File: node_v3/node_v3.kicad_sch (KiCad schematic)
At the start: 33 parts, among them J1 Conn_Coaxial, J10 Conn_01x02_Pin, J11 Conn_01x02_Pin, J2 Micro_SD_Card, J3 Conn_01x02_Pin, J4 Conn_01x02_Pin, J5 Conn_01x04_Pin, J6 Conn_01x02_Pin, J7 Conn_01x06_Pin, J8 Conn_01x04_Pin, J9 Conn_01x03_Pin, Q1 2N3904, U1 RFM69HCW, U2 Pico, U3 MCP73831-2-OT, U4 ADP2108AUJ-3.3, U5 CAT3200-5

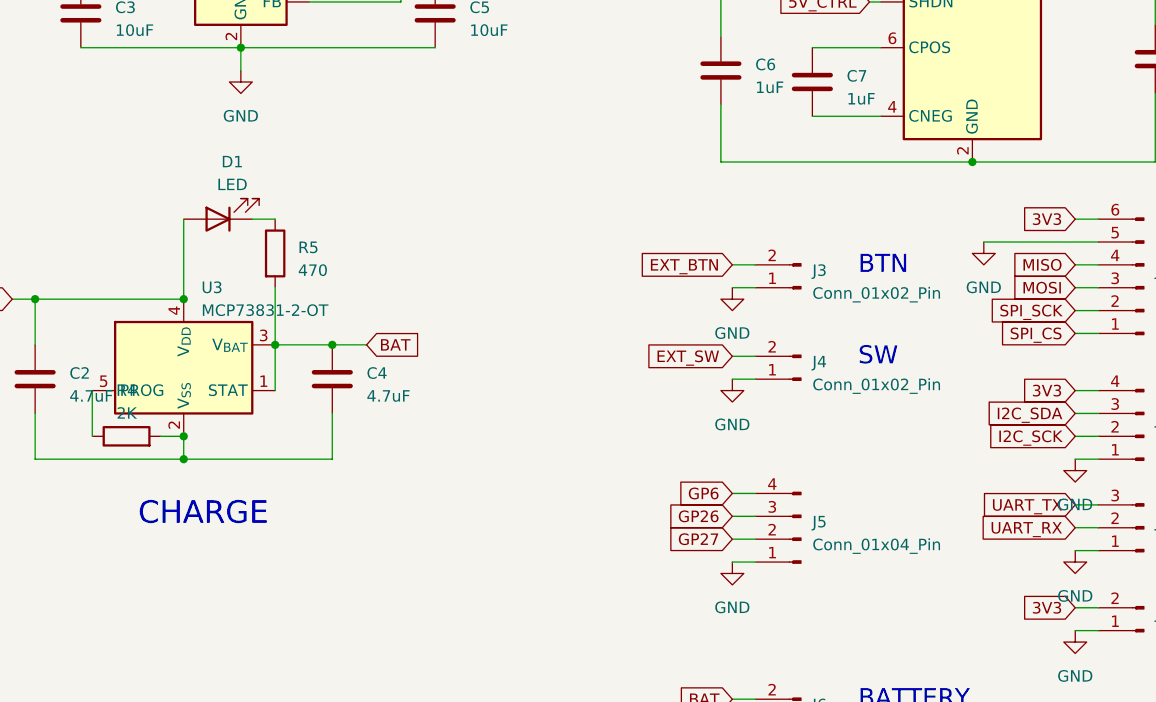
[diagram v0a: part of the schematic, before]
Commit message: added missing grounds
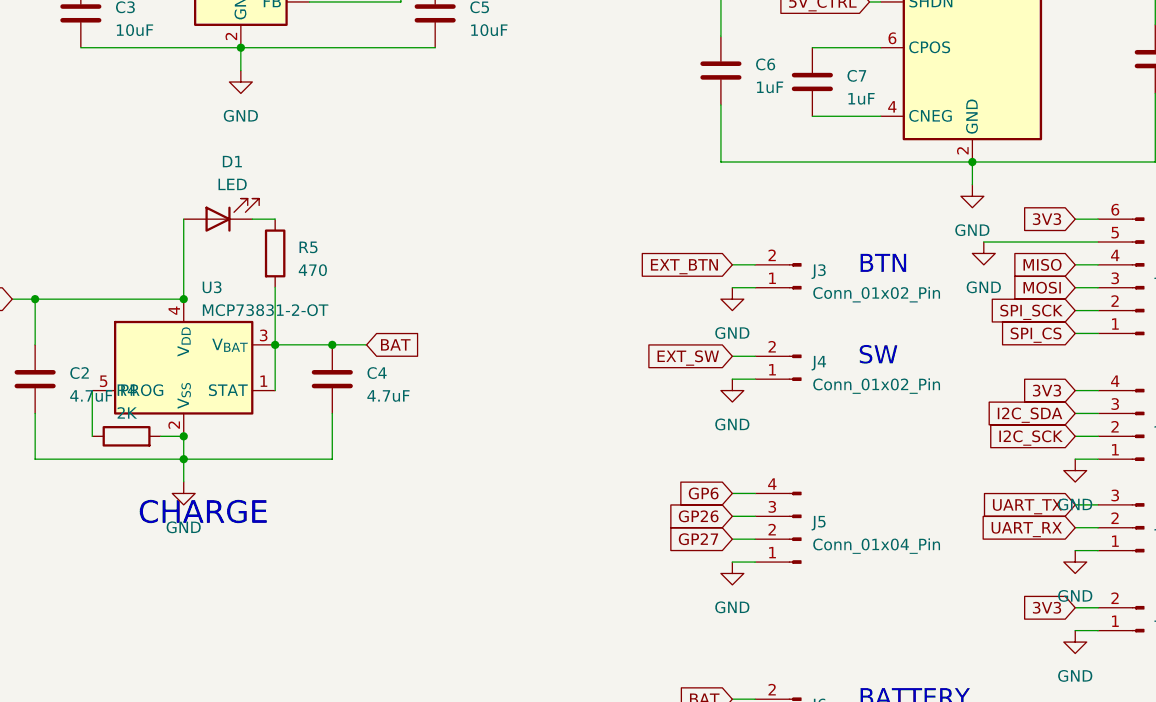
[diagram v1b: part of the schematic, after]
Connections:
- net GND: now also C2.2, C4.2, C6.2, C8.2, R4.2, U3.2 (V_{SS}), U5.2 (GND)
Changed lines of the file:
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@@
+    (stroke (width 0) (type default))
+  )
+  (wire (pts (xy 146.05 97.79) (xy 146.05 100.33))
     (stroke (width 0) (type default))
   )
@@
   )
   (wire (pts (xy 100.33 135.89) (xy 100.33 138.43))
+    (stroke (width 0) (type default))
+  )
+  (wire (pts (xy 233.68 64.77) (xy 233.68 67.31))
     (stroke (width 0) (type default))
   )
@@
         )
       )
+    )
+  )
+  (symbol (lib_id "power:GND") (at 233.68 67.31 0) (unit 1)
+    (in_bom yes) (on_board yes) (dnp no) (fields_autoplaced)
+    (property "Reference" "#PWR019" (at 233.68 73.66 0)
+      (effects (font (size 1.27 1.27)) hide)
+    )
+    (property "Value" "GND" (at 233.68 72.39 0)
+      (effects (font (size 1.27 1.27)))
+    )
+    (property "Footprint" "" (at 233.68 67.31 0)
+      (effects (font (size 1.27 1.27)) hide)
+    )
+    (property "Datasheet" "" (at 233.68 67.31 0)
+      (effects (font (size 1.27 1.27)) hide)
+    )
+    (pin "1")
+    (instances
+      (project "node_v3"
+        (path "/02682326-2508-4e7d-ab0e-a18e4bd4a5b6"
+          (reference "#PWR019") (unit 1)
+        )
+      )
+    )
+  )
+  (symbol (lib_id "power:GND") (at 146.05 100.33 0) (unit 1)
+    (in_bom yes) (on_board yes) (dnp no) (fields_autoplaced)
+    (property "Reference" "#PWR018" (at 146.05 106.68 0)
+      (effects (font (size 1.27 1.27)) hide)
+    )
+    (property "Value" "GND" (at 146.05 105.41 0)
+      (effects (font (size 1.27 1.27)))
+    )
+    (property "Footprint" "" (at 146.05 100.33 0)
+      (effects (font (size 1.27 1.27)) hide)
+    )
+    (property "Datasheet" "" (at 146.05 100.33 0)
+      (effects (font (size 1.27 1.27)) hide)
+    )
+    (pin "1")
+    (instances
+      (project "node_v3"
+        (path "/02682326-2508-4e7d-ab0e-a18e4bd4a5b6"
+          (reference "#PWR018") (unit 1)
+        )
+      )

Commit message: replaced pico with rp2040
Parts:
- removed U2: Pico, MCU_RaspberryPi_and_Boards:RPi_Pico_SMD_TH, symbol MCU_RaspberryPi_and_Boards:Pico
- added C10, C11, C12, C13, C14, C15, C17, C18, C20, C9: 100n, symbol Device:C
- added C16, C19: 1u, symbol Device:C
- added C21, C22: 15p, symbol Device:C
- added J12: USB_BOOT', Connector_PinHeader_2.54mm:PinHeader_1x02_P2.54mm_Vertical, symbol Connector:Conn_01x02_Pin
- added J13: Conn_01x03_Pin, Connector_PinHeader_2.54mm:PinHeader_1x03_P2.54mm_Vertical, symbol Connector:Conn_01x03_Pin
- added J14: Conn_01x02_Pin, Connector_PinHeader_2.54mm:PinHeader_1x02_P2.54mm_Vertical, symbol Connector:Conn_01x02_Pin
- added P1: USB_C_Plug_USB2.0, symbol Connector:USB_C_Plug_USB2.0
- added R10: 1k, symbol Device:R
- added R11: 0, symbol Device:R
- added R7, R8: 27.4, symbol Device:R
- added R9: DNF, symbol Device:R
- added U6: RP2040, Package_DFN_QFN:QFN-56-1EP_7x7mm_P0.4mm_EP3.2x3.2mm, symbol MCU_RaspberryPi:RP2040
- added U7: W25Q128JVS, Package_SO:SOIC-8_5.23x5.23mm_P1.27mm, symbol Memory_Flash:W25Q128JVS
- added Y1: Crystal, symbol Device:Crystal
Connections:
- net 3V3: now also J7.2 (Pin_2), C10.1, C11.1, C12.1, C13.1, C14.1, C15.1, C16.1, C20.1, C9.1, R9.1, U6.1 (IOVDD), U6.10 (IOVDD), U6.22 (IOVDD), U6.33 (IOVDD), U6.42 (IOVDD), U6.43 (ADC_AVDD), U6.44 (VREG_IN), U6.48 (USB_VDD), U6.49 (IOVDD), U7.8 (VCC); no longer J7.6 (Pin_6)
- net EXT_BTN: now also U6.15 (GPIO12)
- net EXT_SW: now also U6.16 (GPIO13)
- net GND: now also J7.1 (Pin_1), C10.2, C11.2, C12.2, C13.2, C14.2, C15.2, C16.2, C17.2, C18.2, C19.2, C20.2, C21.1, C22.1, C9.2, J12.1 (Pin_1), J13.1 (Pin_1), J14.1 (Pin_1), P1.A1 (GND), P1.A12 (GND), P1.B1 (GND), P1.B12 (GND), R11.2, U6.57 (GND), U7.4 (GND); no longer J7.5 (Pin_5)
- net GP26: now also U6.38 (GPIO26_ADC0)
- net GP27: now also U6.39 (GPIO27_ADC1)
- net GP6: now also U6.8 (GPIO6)
- net I2C_SCK: now also U6.7 (GPIO5)
- net I2C_SDA: now also U6.6 (GPIO4)
- net MISO: now also J7.6 (Pin_6), U6.27 (GPIO16); no longer J7.4 (Pin_4)
- net MOSI: now also J7.5 (Pin_5), U6.30 (GPIO19); no longer J7.3 (Pin_3)
- net RFM_CS: now also U6.28 (GPIO17)
- net RFM_RST: now also U6.31 (GPIO20)
- net SD_CS: now also U6.32 (GPIO21)
- net SPI_CS: now also J7.3 (Pin_3), U6.34 (GPIO22); no longer J7.1 (Pin_1)
- net SPI_SCK: now also J7.4 (Pin_4), U6.29 (GPIO18); no longer J7.2 (Pin_2)
- net UART_RX: now also U6.3 (GPIO1)
- net UART_TX: now also U6.2 (GPIO0)
- net at R1.1: now also U6.14 (GPIO11)
- net at R2.2, R3.1: now also U6.40 (GPIO28_ADC2)
- net CHG renamed VIN
- net VIN: now also J14.2 (Pin_2), P1.A4 (VBUS), P1.A9 (VBUS), P1.B4 (VBUS), P1.B9 (VBUS)
- net TEROS_CTRL renamed 5V_SW
- net 5V_SW: now also U6.4 (GPIO2)
- new net: C21.2, U6.20 (XIN), Y1.2
- new net: R7.2, U6.47 (USB_DP)
- new net: J12.2 (Pin_2), R10.1
- new net: R8.2, U6.46 (USB_DM)
- new net: C22.2, U6.21 (XOUT), Y1.1
- new net: P1.S1 (SHIELD), R11.1
- new net: U6.23 (DVDD), U6.50 (DVDD)
- new net 1V1: C17.1, C18.1, C19.1, U6.45 (VREG_VOUT)
- new net QSPI_CLK: U6.52 (QSPI_SCLK), U7.6 (CLK)
- new net QSPI_CS: R10.2, R9.2, U6.56 (QSPI_SS), U7.1 (~{CS})
- new net QSPI_SD0: U6.53 (QSPI_SD0), U7.5 (DI(IO0))
- new net QSPI_SD1: U6.55 (QSPI_SD1), U7.2 (DO(IO1))
- new net QSPI_SD2: U6.54 (QSPI_SD2), U7.3 (IO2)
- new net QSPI_SD3: U6.51 (QSPI_SD3), U7.7 (IO3)
- new net SWD: J13.3 (Pin_3), U6.25 (SWD)
- new net SWDCLK: J13.2 (Pin_2), U6.24 (SWCLK)
- new net USB+: P1.A6 (D+), R7.1
- new net USB-: P1.A7 (D-), R8.1
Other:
- note added: "3.3V SUPPLY"
- note added: "3V3 OUT"
- note added: "5V SUPPLY"
- note added: "5V SWITCHABLE"
- note added: "DEBUG"
- note added: "GPIO"
- note added: "QSPI FLASH"
- note added: "SPI0"
- note added: "VIN"
- note removed: "3.3V"
- note removed: "3V3_PIN"
- note removed: "5V"
- note removed: "MCU"
- note removed: "SPI"
- note removed: "Teros Sensor"
- moved on the sheet: C1, C2, C3, C4, C5, C6, C7, C8, D1, J1, J10, J11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

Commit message: progress
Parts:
- added C23: C, symbol Device:C
- added U2: MCP7940N-xSN, symbol Timer_RTC:MCP7940N-xSN
- added Y2: Crystal, symbol Device:Crystal
- C21, C22: footprint (none) -> Capacitor_SMD:C_0603_1608Metric_Pad1.08x0.95mm_HandSolder
- J1: footprint Connector_Coaxial:SMA_Amphenol_132289_EdgeMount -> Connector_Coaxial:SMA_Samtec_SMA-J-P-X-ST-EM1_EdgeMount
- Q1: footprint PCM_Package_TO_SOT_THT_AKL:TO-92_Inline -> Package_TO_SOT_SMD:SC-59_Handsoldering
- R10, R11, R7, R8, R9: footprint (none) -> Resistor_SMD:R_0805_2012Metric_Pad1.20x1.40mm_HandSolder
- Y1: footprint (none) -> kicad-footprints-master:XTAL_M445
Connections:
- net 3V3: now also C23.1, U2.8 (VCC)
- net GND: now also J2.9 (SHIELD), C23.2, U2.4 (VSS)
- net I2C_SCK: now also U2.6 (SCL)
- net I2C_SDA: now also U2.5 (SDA)
- net RTC_MFP: now reaches U6.18 (GPIO15)
- net RTC_MFP: now also U2.7 (MFP)
- new net: U2.1 (X1), Y2.1
- new net: U2.2 (X2), Y2.2
- new net RTC_BAT: U2.3 (VBAT)
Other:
- note added: "RTC"

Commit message: moved stuff around, replaced headers, usb, footprints, started pcb
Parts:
- removed J11, J3, J4: Conn_01x02_Pin, Connector_PinHeader_2.54mm:PinHeader_1x02_P2.54mm_Vertical, symbol Connector:Conn_01x02_Pin
- removed J12: USB_BOOT', Connector_PinHeader_2.54mm:PinHeader_1x02_P2.54mm_Vertical, symbol Connector:Conn_01x02_Pin
- removed J5, J8: Conn_01x04_Pin, Connector_PinHeader_2.54mm:PinHeader_1x04_P2.54mm_Vertical, symbol Connector:Conn_01x04_Pin
- removed J7: Conn_01x06_Pin, Connector_PinHeader_2.54mm:PinHeader_1x06_P2.54mm_Vertical, symbol Connector:Conn_01x06_Pin
- removed J9: Conn_01x03_Pin, Connector_PinHeader_2.54mm:PinHeader_1x03_P2.54mm_Vertical, symbol Connector:Conn_01x03_Pin
- removed P1: USB_C_Plug_USB2.0, symbol Connector:USB_C_Plug_USB2.0
- added C24: .1u, Capacitor_SMD:C_0402_1005Metric, symbol Device:C
- added C25: 10u, Capacitor_SMD:C_0805_2012Metric_Pad1.18x1.45mm_HandSolder, symbol Device:C
- added J12: 12402012E212A, custom:AMPHENOL_12402012E212A, symbol custom:12402012E212A
- added J15: Conn_01x16_Pin, Connector_PinHeader_2.54mm:PinHeader_1x16_P2.54mm_Vertical, symbol Connector:Conn_01x16_Pin
- added SW1, SW2: PTS526, custom:PTS526, symbol custom:PTS526
- C1: footprint Capacitor_SMD:C_0805_2012Metric_Pad1.18x1.45mm_HandSolder -> Capacitor_SMD:C_0402_1005Metric
- C10, C11, C12, C13, C14, C15, C17, C18, C20, C9: footprint (none) -> Capacitor_SMD:C_0402_1005Metric_Pad0.74x0.62mm_HandSolder
- C16, C19: footprint (none) -> Capacitor_SMD:C_0805_2012Metric_Pad1.18x1.45mm_HandSolder
- C21, C22: footprint Capacitor_SMD:C_0603_1608Metric_Pad1.08x0.95mm_HandSolder -> Capacitor_SMD:C_0402_1005Metric_Pad0.74x0.62mm_HandSolder
- C23: value C -> 10u; footprint (none) -> Capacitor_SMD:C_0805_2012Metric_Pad1.18x1.45mm_HandSolder
- J10: value Conn_01x02_Pin -> 3V3OUT
- J13: value Conn_01x03_Pin -> DBG
- J14: value Conn_01x02_Pin -> VIN
- J6: value Conn_01x02_Pin -> BAT
- U2: footprint (none) -> Package_SO:SOIC-8_3.9x4.9mm_P1.27mm
- Y1: value Crystal -> 445C35A12M00000
- Y2: value Crystal -> SC32S-7PF20PPM; footprint (none) -> custom:SC-32S
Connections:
- net 3V3: now also C24.1, C25.1, J15.2 (Pin_2)
- net 5V: now also Q1.3 (C)
- net 5V_SW: now also Q1.1 (E), J15.3 (Pin_3)
- net GND: now also C24.2, C25.2, J12.A1_B12 (GND), J12.B1_A12 (GND__1), J15.1 (Pin_1), SW1.1, SW1.2, SW2.1, SW2.2; no longer Q1.1 (E)
- net GP26: now also J15.13 (Pin_13)
- net GP27: now also J15.12 (Pin_12)
- net GP6: now also J15.14 (Pin_14)
- net I2C_SCK: now also J15.6 (Pin_6)
- net I2C_SDA: now also J15.7 (Pin_7)
- net MISO: now also J15.11 (Pin_11)
- net MOSI: now also J15.10 (Pin_10)
- net SPI_CS: now also J15.8 (Pin_8)
- net SPI_SCK: now also J15.9 (Pin_9)
- net UART_RX: now also J15.4 (Pin_4)
- net UART_TX: now also J15.5 (Pin_5)
- net USB+: now also J12.A6 (D+_A), J12.B6 (D+_B)
- net USB-: now also J12.A7 (D-_A), J12.B7 (D-_B)
- net VIN: now also J12.A4_B9 (VBUS), J12.B4_A9 (VBUS__1)
- net at R10.1: now also SW1.3, SW1.4
- net at R11.1: now also J12.SH1 (SHIELD), J12.SH2 (SHIELD__1), J12.SH3 (SHIELD__2), J12.SH4 (SHIELD__3)
- net at U6.26 (RUN): now also SW2.3, SW2.4
- net EXT_BTN renamed EXT_SW1
- net EXT_SW1: now also J15.16 (Pin_16)
- net EXT_SW renamed EXT_SW2
- net EXT_SW2: now also J15.15 (Pin_15)
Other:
- note added: "IO"
- note added: "RP2040"
- note added: "SD CARD"
- note added: "USB TYPE-C"
- note removed: "5V SWITCHABLE"
- note removed: "BTN"
- note removed: "GPIO"
- note removed: "I2C"
- note removed: "SPI0"
- note removed: "SW"
- note removed: "UART"
- moved on the sheet: Q1, R6

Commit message: finished? the pcb design - need to look into sd card stuff first
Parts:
- added BT1: Battery_Cell, custom:BAT-HLD-001-THM_TEC, symbol Device:Battery_Cell
- added C26, C27: 6p, Capacitor_SMD:C_0603_1608Metric_Pad1.08x0.95mm_HandSolder, symbol Device:C
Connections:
- net 5V_SW: no longer Q1.1 (E)
- net GND: now also BT1.2 (-), C26.2, C27.2
- net at U2.1 (X1), Y2.1: now also C26.1
- net at U2.2 (X2), Y2.2: now also C27.1
- net RTC_BAT: no longer names the net of U2.3 (VBAT)
- net RTC_BAT: now also BT1.1 (+)
- new net 5V_OUT: Q1.1 (E)

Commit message: not finished yet
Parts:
- added R12, R13, R14, R15: R, Resistor_SMD:R_0805_2012Metric_Pad1.20x1.40mm_HandSolder, symbol Device:R
- U1: footprint RF_Module:HOPERF_RFM69HW -> custom:HOPERF_RFM9XW_SMD
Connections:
- net 3V3: now also R12.1, R13.1, R14.1, R15.1
- net GND: no longer J2.1 (DAT2), J2.8 (DAT1)
- net MISO: now also R13.2
- net SD_CS: now also R14.2
- new net: J2.1 (DAT2), R12.2
- new net: J2.8 (DAT1), R15.2

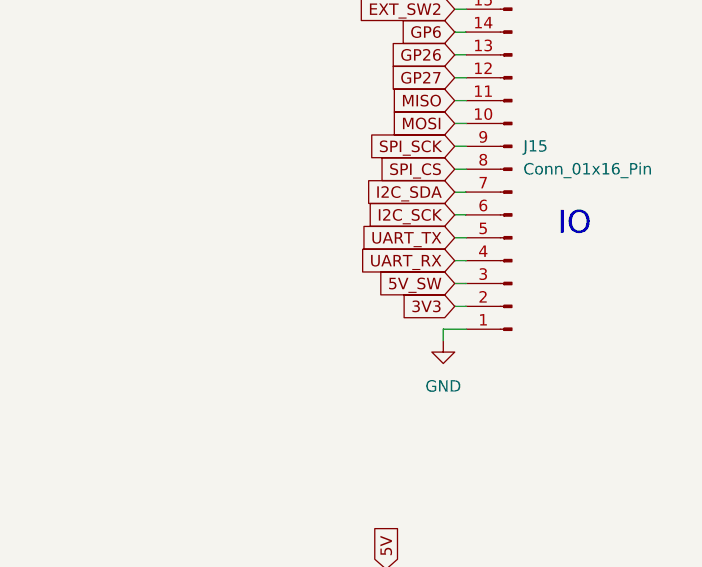
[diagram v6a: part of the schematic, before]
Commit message: fixed the rfm footprint, fixed via sizes. need to adjust some vias to be bigger
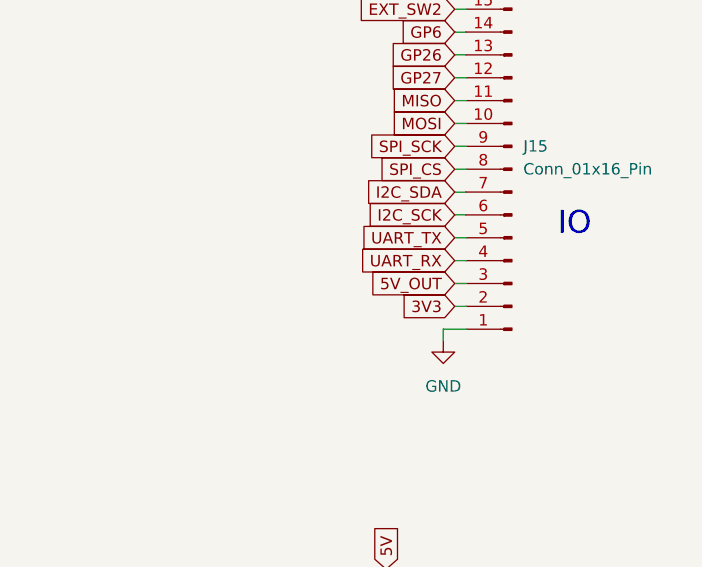
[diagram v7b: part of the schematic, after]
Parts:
- U1: footprint custom:HOPERF_RFM9XW_SMD -> RF_Module:HOPERF_RFM9XW_SMD
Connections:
- net 5V_OUT: now also J15.3 (Pin_3)
- net 5V_SW: no longer J15.3 (Pin_3)
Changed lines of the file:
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@@
     )
   )
-  (global_label "5V_SW" (shape input) (at 379.73 93.98 180) (fields_autoplaced)
-    (effects (font (size 1.27 1.27)) (justify right))
-    (property "Intersheetrefs" "${INTERSHEET_REFS}" (at 370.8182 93.98 0)
+  (global_label "5V_OUT" (shape input) (at 379.73 93.98 180) (fields_autoplaced)
+    (effects (font (size 1.27 1.27)) (justify right))
+    (property "Intersheetrefs" "${INTERSHEET_REFS}" (at 369.8505 93.98 0)
       (effects (font (size 1.27 1.27)) (justify right) hide)
     )
@@
       (effects (font (size 1.27 1.27)) (justify left))
     )
-    (property "Footprint" "custom:HOPERF_RFM9XW_SMD" (at 92.71 63.5 0)
-      (effects (font (size 1.27 1.27)) hide)
-    )
+    (property "Footprint" "RF_Module:HOPERF_RFM9XW_SMD" (at 92.71 63.5 0)
+      (effects (font (size 1.27 1.27)) hide)
+    )
